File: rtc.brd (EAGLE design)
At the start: 27.9 x 29.2 mm, 14 parts, among them U1 MCP79412, Y1 32.768 kHz

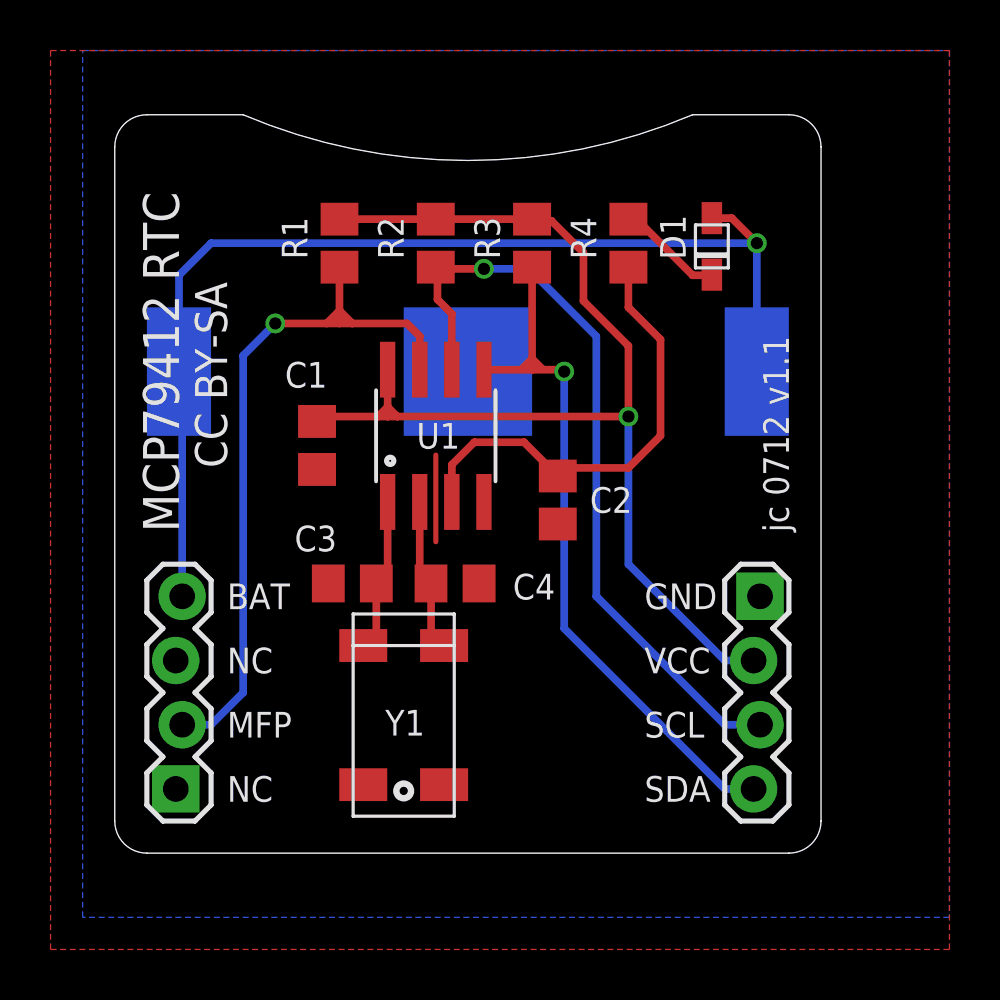
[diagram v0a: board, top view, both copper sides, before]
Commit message: Updated coin cell footprint, R and C footprints, OSHW logo.
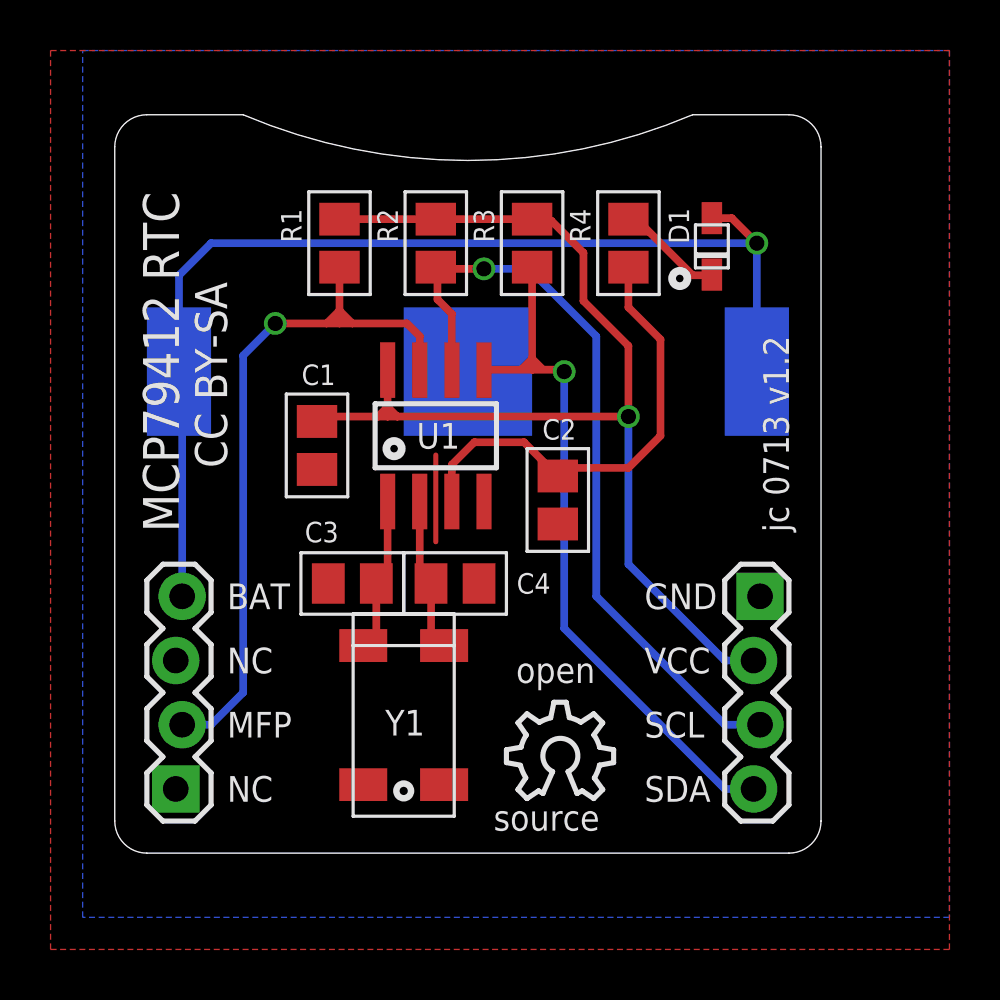
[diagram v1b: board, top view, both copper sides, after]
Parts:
- added LOGO2: OSHW_LOGO_8MILX0150-NT, ohw-logo:OSHW_8X150_NOTEXT
- C1, C2, C3, C4: device rcl:C0805 -> _jc:M0805
- R1, R2, R3, R4: device rcl:R0805 -> _jc:M0805
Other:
- board text added: "jc 0713 v1.2"
- board text added: "open"
- board text added: "source"
- board text removed: "0000"
- board text removed: "jc 0712 v1.1"

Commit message: Update README, add LICENSE and other misc files. Regenerate Gerber files.
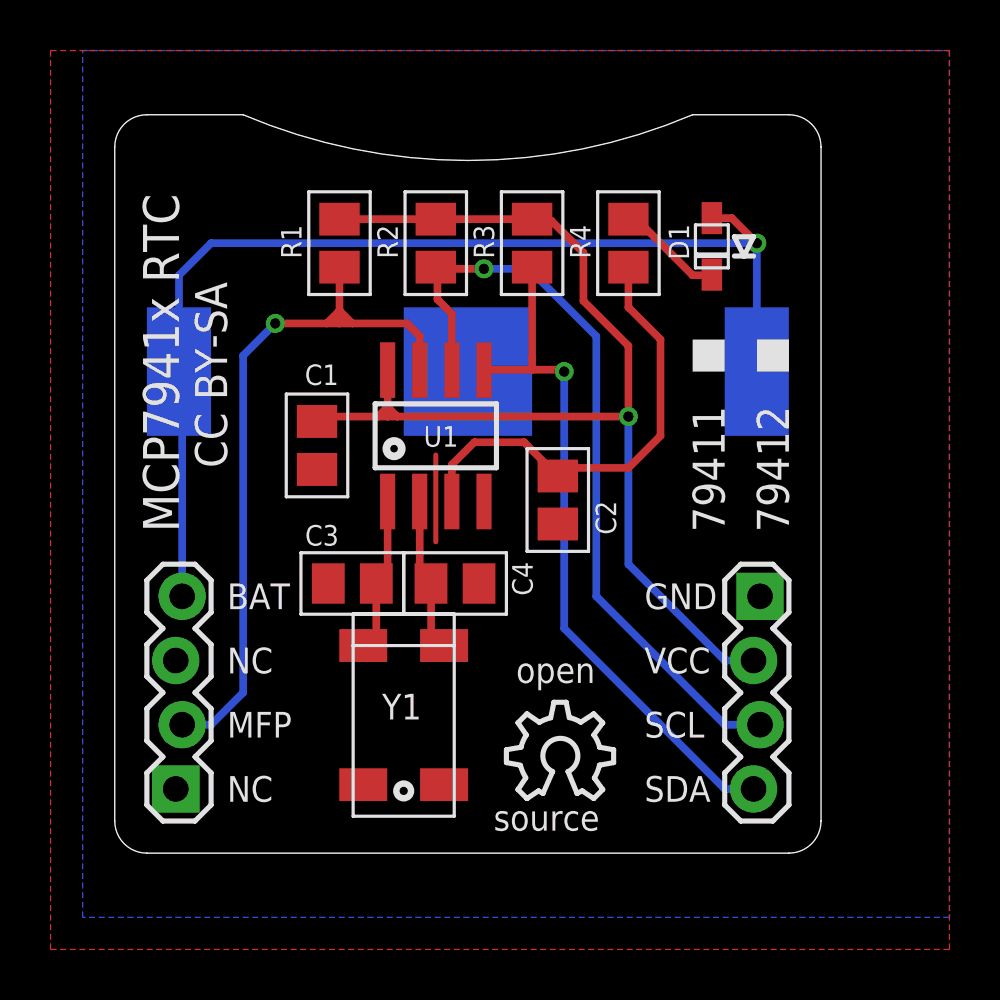
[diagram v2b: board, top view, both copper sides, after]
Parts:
- D1: device _jc:SOD-323F -> _jc:SOD-323F-A
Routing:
- net SDA: track 28.6 -> 27.6 mm
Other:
- board text added: "79411"
- board text added: "79412"
- board text added: "MCP7941x"
- board text added: "MCP7941x RTC"
- board text added: "jc 0314 v1.3"
- board text removed: "MCP79412"
- board text removed: "MCP79412 RTC"
- board text removed: "jc 0713 v1.2"
